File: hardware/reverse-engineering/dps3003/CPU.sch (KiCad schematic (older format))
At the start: 30 parts, among them Q3 SS8050(Y1)

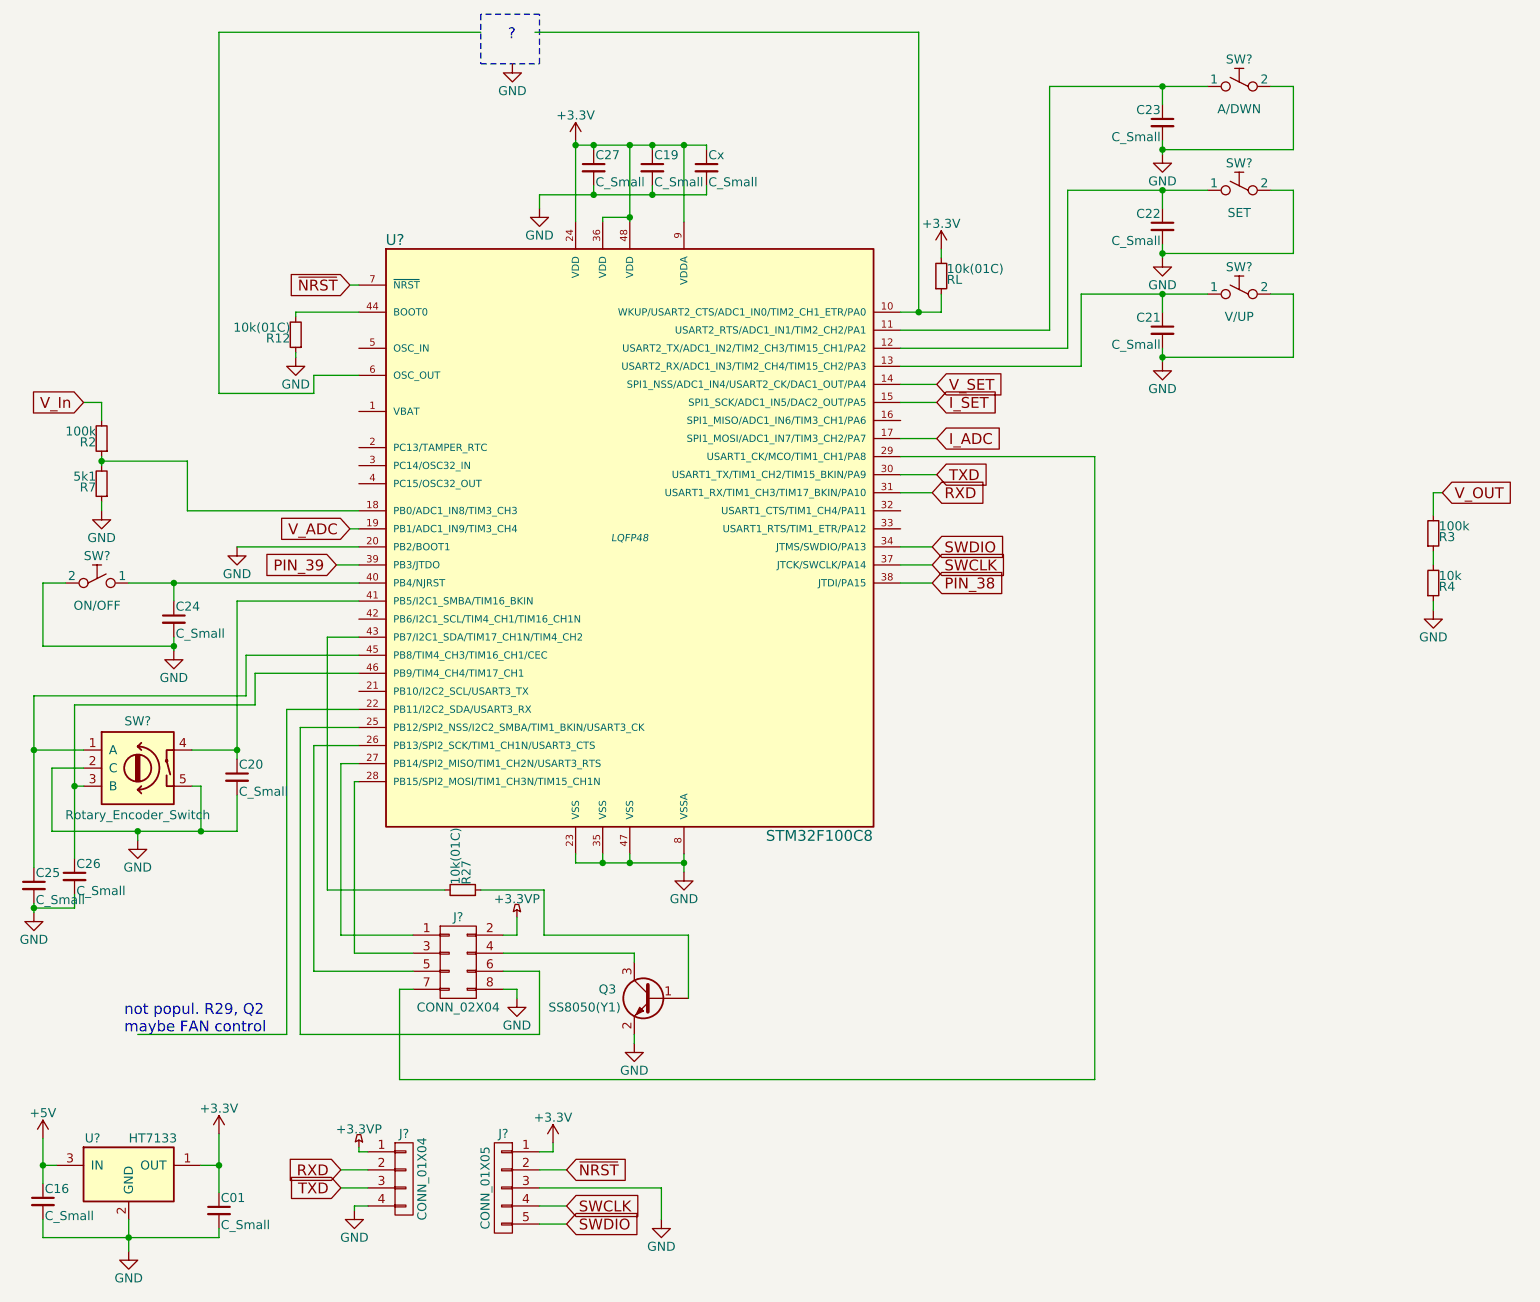
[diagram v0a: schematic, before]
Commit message: Fixed #61
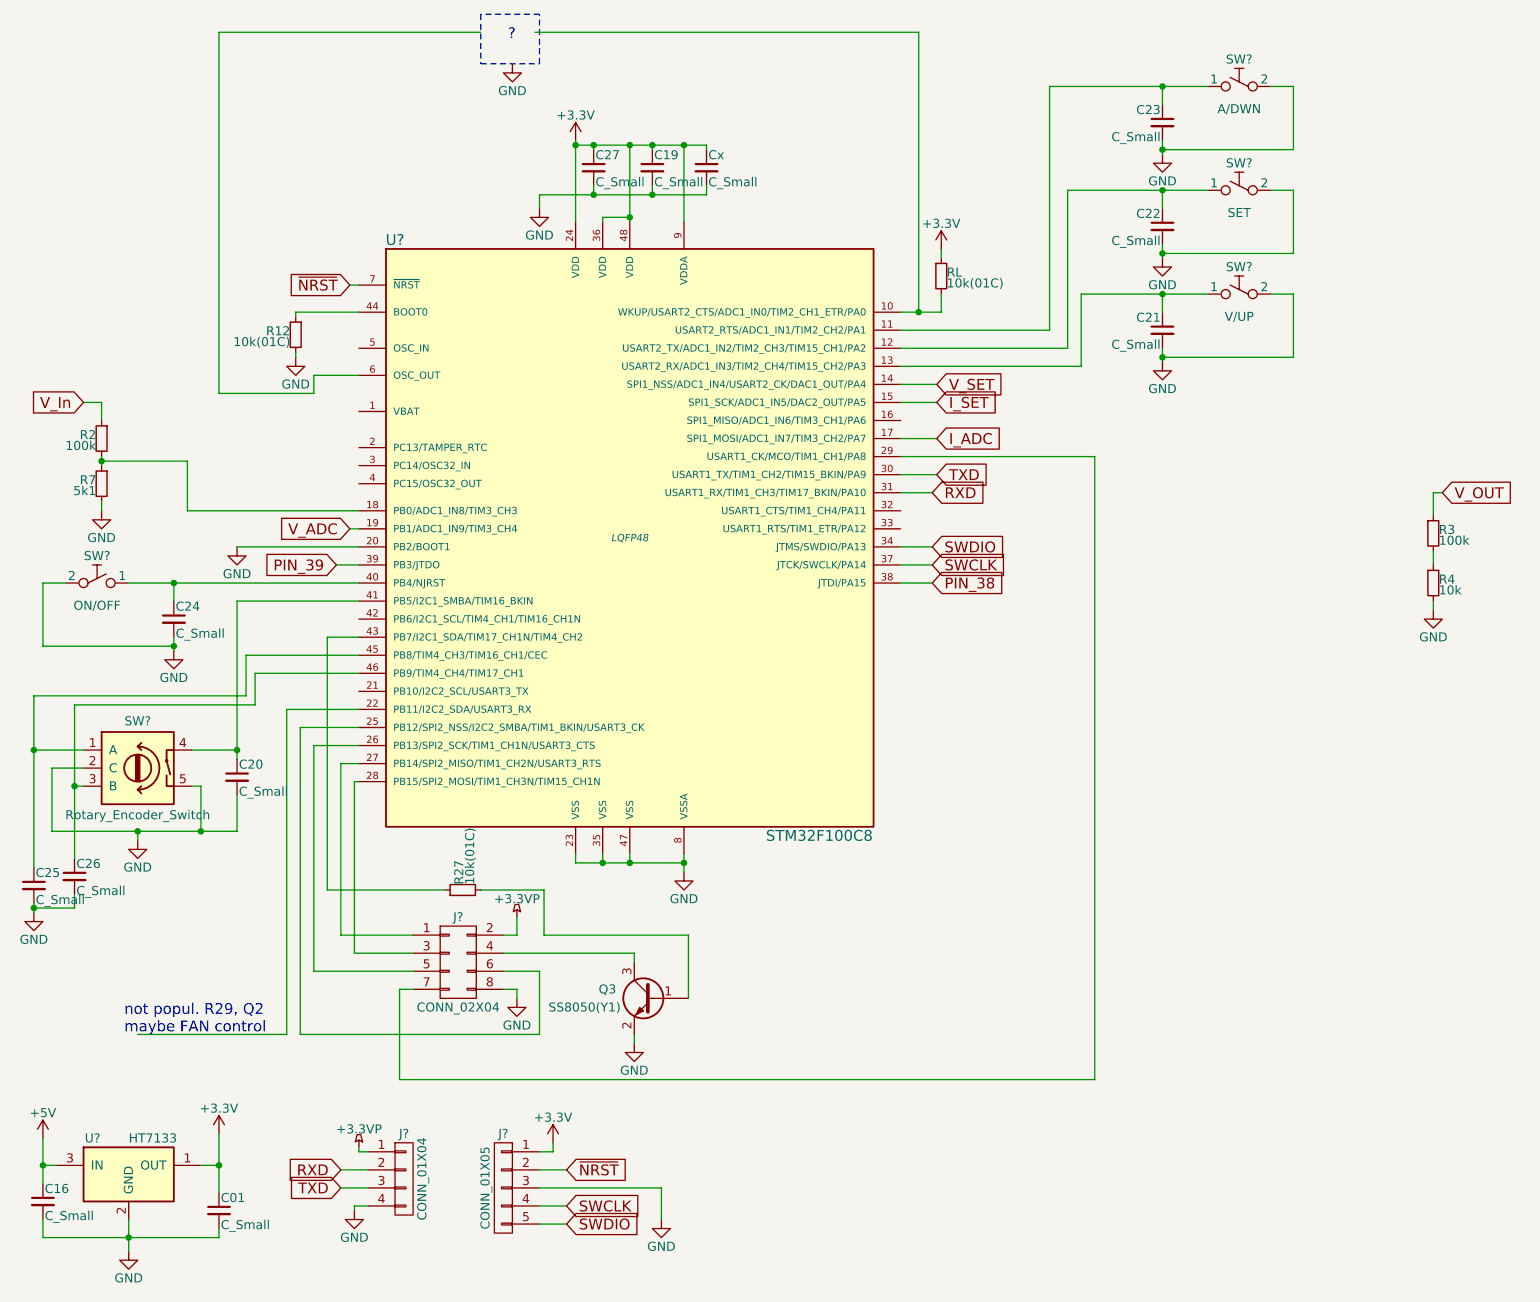
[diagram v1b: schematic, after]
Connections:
- net +3V3: now also RL.1; no longer RL.2
- net GND: now also R12.2, R4.2, R7.2; no longer R12.1, R4.1, R7.1
- net V_In: now also R2.1; no longer R2.2
- net V_OUT: now also R3.1; no longer R3.2
- net at U?.10 (WKUP/USART2_CTS/ADC1_IN0/TIM2_CH1_ETR/PA0): now also RL.2; no longer RL.1
- net at U?.43 (PB7/I2C1_SDA/TIM17_CH1N/TIM4_CH2): now also R27.1; no longer R27.2
- net at U?.44 (BOOT0): now also R12.1; no longer R12.2
- net at Q3.1 (B): now also R27.2; no longer R27.1
- new net: R2.2, R7.1, U?.18 (PB0/ADC1_IN8/TIM3_CH3)
- new net: R3.2, R4.1
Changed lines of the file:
@@
 LIBS:my_sensors
 LIBS:my_transistors
-LIBS:DPS3203-cache
+LIBS:DPS3003-cache
 EELAYER 25 0
 EELAYER END
@@
 $EndComp
 Wire Wire Line
-	650  6950 650  7100
-Wire Wire Line
-	650  7100 650  7200
+	650  6950 650  7200
 Wire Wire Line
 	725  7100 650  7100
@@
 	650  7400 650  7500
 Wire Wire Line
-	650  7500 1125 7500
-Wire Wire Line
-	1125 7500 1625 7500
-Wire Wire Line
-	1125 7400 1125 7500
-Wire Wire Line
-	1125 7500 1125 7575
+	650  7500 1625 7500
+Wire Wire Line
+	1125 7400 1125 7575
 Connection ~ 1125 7500
 $Comp
@@
 	1525 7100 1625 7100
 Wire Wire Line
-	1625 6925 1625 7100
-Wire Wire Line
-	1625 7100 1625 7250
+	1625 6925 1625 7250
 Wire Wire Line
 	1625 7500 1625 7450
@@
 $EndComp
 Wire Wire Line
-	3600 1425 3600 1450
-Wire Wire Line
-	3600 1450 3600 1875
+	3600 1425 3600 1875
 Wire Wire Line
 	3700 1475 3700 1450
 Wire Wire Line
-	3600 1450 3700 1450
-Wire Wire Line
-	3700 1450 3900 1450
-Wire Wire Line
-	3900 1450 4025 1450
-Wire Wire Line
-	4025 1450 4200 1450
-Wire Wire Line
-	4200 1450 4325 1450
+	3600 1450 4325 1450
 Connection ~ 3600 1450
 $Comp
@@
 	3750 1850 3900 1850
 Wire Wire Line
-	3900 1450 3900 1850
-Wire Wire Line
-	3900 1850 3900 1875
+	3900 1450 3900 1875
 Connection ~ 3900 1450
 $Comp
@@
 	3400 1800 3400 1725
 Wire Wire Line
-	3400 1725 3700 1725
-Wire Wire Line
-	3700 1725 4025 1725
-Wire Wire Line
-	4025 1725 4325 1725
+	3400 1725 4325 1725
 Wire Wire Line
 	4025 1725 4025 1675
@@
 $EndComp
 Wire Wire Line
-	6400 2275 6850 2275
-Wire Wire Line
-	6850 2275 7100 2275
+	6400 2275 7100 2275
 Wire Wire Line
 	6850 2275 6850 2375
 Wire Wire Line
-	6850 2575 6850 2625
-Wire Wire Line
-	6850 2625 6850 2650
+	6850 2575 6850 2650
 Wire Wire Line
 	6850 2625 7575 2625
@@
 $EndComp
 Wire Wire Line
-	6325 1700 6850 1700
-Wire Wire Line
-	6850 1700 7100 1700
+	6325 1700 7100 1700
 Wire Wire Line
 	6850 1700 6850 1800
 Wire Wire Line
-	6850 2000 6850 2050
-Wire Wire Line
-	6850 2050 6850 2075
+	6850 2000 6850 2075
 Wire Wire Line
 	6850 2050 7575 2050
@@
 $EndComp
 Wire Wire Line
-	6225 1125 6850 1125
-Wire Wire Line
-	6850 1125 7100 1125
+	6225 1125 7100 1125
 Wire Wire Line
 	6850 1125 6850 1225
 Wire Wire Line
-	6850 1425 6850 1475
-Wire Wire Line
-	6850 1475 6850 1500
+	6850 1425 6850 1500
 Wire Wire Line
 	6850 1475 7575 1475
@@
 $EndComp
 Wire Wire Line
-	1125 3875 1375 3875
-Wire Wire Line
-	1375 3875 2400 3875
+	1125 3875 2400 3875
 Wire Wire Line
 	1375 3875 1375 3975
 Wire Wire Line
-	1375 4175 1375 4225
-Wire Wire Line
-	1375 4225 1375 4250
+	1375 4175 1375 4250
 Wire Wire Line
 	1375 4225 650  4225
@@
 	1475 4800 1725 4800
 Wire Wire Line
-	1725 3975 1725 4800
-Wire Wire Line
-	1725 4800 1725 4850
+	1725 3975 1725 4850
 Wire Wire Line
 	1725 3975 2400 3975
@@
 	1175 5300 1175 5250
 Wire Wire Line
-	700  5250 1175 5250
-Wire Wire Line
-	1175 5250 1525 5250
-Wire Wire Line
-	1525 5250 1725 5250
+	700  5250 1725 5250
 Wire Wire Line
 	1525 5250 1525 5000
@@
 $EndComp
 Wire Wire Line
-	600  5650 600  5675
-Wire Wire Line
-	600  5675 600  5700
+	600  5650 600  5700
 Wire Wire Line
 	600  5675 825  5675
@@
 	1775 4500 600  4500
 Wire Wire Line
-	600  4500 600  4800
-Wire Wire Line
-	600  4800 600  5450
+	600  4500 600  5450
 Wire Wire Line
 	875  4800 600  4800
@@
 	875  5000 825  5000
 Wire Wire Line
-	825  4550 825  5000
-Wire Wire Line
-	825  5000 825  5400
+	825  4550 825  5400
 Wire Wire Line
 	825  4550 1825 4550
@@
 F 3 "" H 2975 5575 50  0001 C CNN
 	1    2975 5575
-	0    1    -1   0
+	0    -1   -1   0
 $EndComp
 Wire Wire Line
@@
 $EndComp
 Wire Wire Line
-	4200 5375 4200 5425
-Wire Wire Line
-	4200 5425 4200 5475
-Wire Wire Line
-	3600 5425 3750 5425
-Wire Wire Line
-	3750 5425 3900 5425
-Wire Wire Line
-	3900 5425 4200 5425
+	4200 5375 4200 5475
+Wire Wire Line
+	3600 5425 4200 5425
 Wire Wire Line
 	3600 5425 3600 5375
@@
 F 3 "" H 8350 3600 50  0001 C CNN
 	1    8350 3600
-	1    0    0    1
+	1    0    0    -1
 $EndComp
 $Comp
@@
 F 3 "" H 8350 3875 50  0001 C CNN
 	1    8350 3875
-	1    0    0    1
+	1    0    0    -1
 $EndComp
 $Comp
@@
 F 3 "" H 975 3075 50  0001 C CNN
 	1    975  3075
-	-1   0    0    1
+	-1   0    0    -1
 $EndComp
 $Comp
@@
 F 3 "" H 975 3325 50  0001 C CNN
 	1    975  3325
-	-1   0    0    1
+	-1   0    0    -1
 $EndComp
 $Comp
@@
 	975  2875 975  2975
 Wire Wire Line
-	975  3175 975  3200
-Wire Wire Line
-	975  3200 975  3225
+	975  3175 975  3225
 Wire Wire Line
 	975  3425 975  3475
@@
 F 3 "" H 2050 2500 50  0001 C CNN
 	1    2050 2500
-	-1   0    0    1
+	-1   0    0    -1
 $EndComp
 Wire Wire Line
@@
 	5500 825  5500 2375
 Wire Wire Line
-	5400 2375 5500 2375
-Wire Wire Line
-	5500 2375 5625 2375
+	5400 2375 5625 2375
 $Comp
 L R_Small RL
@@
 F 3 "" H 5625 2175 50  0001 C CNN
 	1    5625 2175
-	1    0    0    1
-$EndComp
-$Comp
+	1    0    0    -1
+$EndComp
+$Comp
